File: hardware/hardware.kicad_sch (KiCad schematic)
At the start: 22 parts, among them J1 Screw_Terminal_01x02, J2 Screw_Terminal_01x02, J3 Screw_Terminal_01x02, K1 RM85-2011-35-1005, K2 RM85-2011-35-1005, Q1 BC337, Q2 BC337, U1 XIAO-ESP32-C6, U2 DS18B20

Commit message: Started working on PCB
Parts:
- removed D3, D4: LED, LED_THT:LED_D5.0mm, symbol Device:LED
- removed R7, R8: 100R, Resistor_THT:R_Axial_DIN0204_L3.6mm_D1.6mm_P7.62mm_Horizontal, symbol Device:R
- D1, D2: footprint Diode_THT:D_DO-41_SOD81_P10.16mm_Horizontal -> Diode_THT:D_A-405_P7.62mm_Horizontal

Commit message: Started working on new PCB layout
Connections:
- net RELAY_B_IN: now reaches K2.11 (COM_1)
- net RELAY_B_IN: now also J3.1 (Pin_1), K2.21 (COM_2)
- net RELAY_B_OUT: now reaches K2.14 (NO_1)
- net RELAY_B_OUT: now also J3.2 (Pin_2), K2.24 (NO_2)
- net RELAY_A_IN: now reaches J2.1 (Pin_1)
- net RELAY_A_IN: now also K1.11 (COM_1), K1.21 (COM_2)
- net RELAY_A_OUT: now reaches J2.2 (Pin_2)
- net RELAY_A_OUT: now also K1.14 (NO_1), K1.24 (NO_2)

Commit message: New layout with new screw terminals
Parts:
- J1, J2, J3: footprint Degson Electronics:SHDR2W100P0X500_1X2_1000X780X1020P -> Degson Electronics:DG1285002P14
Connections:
- net LED_A is gone; now on net TEMP_SENSOR_DATA: U1.3 (GPIO2/A2/D2)
- net RELAY_A_CTRL: now also U1.10 (GPIO20/D9/MISO); no longer U1.1 (GPIO0/A0/D0)
- net RELAY_B_CTRL: now also U1.9 (GPIO19/D8/SCK); no longer U1.2 (GPIO1/A1/D1)
- net TEMP_SENSOR_DATA: no longer U1.5 (GPIO22/D4/SDA)
- net LED_B: no longer names the net of U1.4 (GPIO21/D3)
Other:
- moved on the sheet: J1, J2, J3
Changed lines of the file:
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@@
 	(wire
 		(pts
-			(xy 44.45 39.37) (xy 50.8 39.37)
-		)
-		(stroke
-			(width 0)
-			(type default)
-		)
-	)
-	(wire
-		(pts
 			(xy 68.58 134.62) (xy 72.39 134.62)
 		)
@@
 	(wire
 		(pts
-			(xy 201.93 116.84) (xy 207.01 116.84)
+			(xy 179.07 107.95) (xy 184.15 107.95)
 		)
 		(stroke
@@
 	(wire
 		(pts
-			(xy 201.93 119.38) (xy 207.01 119.38)
+			(xy 179.07 110.49) (xy 184.15 110.49)
 		)
 		(stroke
@@
 	(wire
 		(pts
+			(xy 100.33 46.99) (xy 105.41 46.99)
+		)
+		(stroke
+			(width 0)
+			(type default)
+		)
+	)
+	(wire
+		(pts
 			(xy 99.06 74.93) (xy 104.14 74.93)
 		)
@@
 	(wire
 		(pts
-			(xy 201.93 144.78) (xy 207.01 144.78)
+			(xy 44.45 35.56) (xy 50.8 35.56)
 		)
 		(stroke
@@
 	(wire
 		(pts
-			(xy 201.93 129.54) (xy 207.01 129.54)
+			(xy 179.07 135.89) (xy 184.15 135.89)
 		)
 		(stroke
@@
 	(wire
 		(pts
-			(xy 44.45 35.56) (xy 50.8 35.56)
+			(xy 179.07 120.65) (xy 184.15 120.65)
+		)
+		(stroke
+			(width 0)
+			(type default)
+		)
+	)
+	(wire
+		(pts
+			(xy 100.33 43.18) (xy 105.41 43.18)
 		)
 		(stroke
@@
 	(wire
 		(pts
-			(xy 201.93 132.08) (xy 207.01 132.08)
+			(xy 179.07 123.19) (xy 184.15 123.19)
 		)
 		(stroke
@@
 	(wire
 		(pts
-			(xy 44.45 43.18) (xy 50.8 43.18)
-		)
-		(stroke
-			(width 0)
-			(type default)
-		)
-	)
-	(wire
-		(pts
 			(xy 121.92 35.56) (xy 121.92 31.75)
 		)
@@
 	(wire
 		(pts
-			(xy 201.93 142.24) (xy 207.01 142.24)
+			(xy 179.07 133.35) (xy 184.15 133.35)
 		)
 		(stroke
@@
 	(global_label "TEMP_SENSOR_DATA"
 		(shape input)
-		(at 44.45 43.18 180)
+		(at 44.45 35.56 180)
 		(fields_autoplaced yes)
 		(effects
@@
 		)
 		(property "Intersheetrefs" "${INTERSHEET_REFS}"
-			(at 22.7778 43.18 0)
+			(at 22.7778 35.56 0)
 			(effects
 				(font
@@
 	(global_label "230VAC_N"
 		(shape input)
-		(at 201.93 119.38 180)
+		(at 179.07 110.49 180)
 		(fields_autoplaced yes)
 		(effects
@@
 		)
 		(property "Intersheetrefs" "${INTERSHEET_REFS}"
-			(at 189.571 119.38 0)
+			(at 166.711 110.49 0)
 			(effects
 				(font
@@
 		)
 	)
-	(global_label "RELAY_B_CTRL"
-		(shape input)
-		(at 44.45 31.75 180)
-		(fields_autoplaced yes)
-		(effects
-			(font
-				(size 1.27 1.27)
-			)
-			(justify right)
-		)
-		(property "Intersheetrefs" "${INTERSHEET_REFS}"
-			(at 28.0996 31.75 0)
-			(effects
-				(font
-					(size 1.27 1.27)
-				)
-				(justify right)
-				(hide yes)
-			)
-		)
-	)
-	(global_label "LED_A"
-		(shape input)
-		(at 44.45 35.56 180)
-		(fields_autoplaced yes)
-		(effects
-			(font
-				(size 1.27 1.27)
-			)
-			(justify right)
-		)
-		(property "Intersheetrefs" "${INTERSHEET_REFS}"
-			(at 35.9615 35.56 0)
-			(effects
-				(font
-					(size 1.27 1.27)
-				)
-				(justify right)
-				(hide yes)
-			)
-		)
-	)
-	(global_label "LED_B"
+	(global_label "RELAY_B_OUT"
 		(shape input)
-		(at 44.45 39.37 180)
+		(at 31.75 134.62 180)
 		(fields_autoplaced yes)
 		(effects
@@
 		)
 		(property "Intersheetrefs" "${INTERSHEET_REFS}"
-			(at 35.7801 39.37 0)
+			(at 16.3067 134.62 0)
 			(effects
 				(font
@@
 		)
 	)
-	(global_label "RELAY_B_OUT"
+	(global_label "230VAC_L"
 		(shape input)
-		(at 31.75 134.62 180)
+		(at 179.07 107.95 180)
 		(fields_autoplaced yes)
 		(effects
@@
 		)
 		(property "Intersheetrefs" "${INTERSHEET_REFS}"
-			(at 16.3067 134.62 0)
+			(at 167.0134 107.95 0)
 			(effects
 				(font
@@
 		)
 	)
-	(global_label "230VAC_L"
+	(global_label "RELAY_B_IN"
 		(shape input)
-		(at 201.93 116.84 180)
+		(at 31.75 132.08 180)
 		(fields_autoplaced yes)
 		(effects
@@
 		)
 		(property "Intersheetrefs" "${INTERSHEET_REFS}"
-			(at 189.8734 116.84 0)
+			(at 18 132.08 0)
 			(effects
 				(font
@@
 		)
 	)
-	(global_label "RELAY_B_IN"
+	(global_label "RELAY_A_CTRL"
 		(shape input)
-		(at 31.75 132.08 180)
+		(at 105.41 43.18 0)
 		(fields_autoplaced yes)
 		(effects
@@
 				(size 1.27 1.27)
 			)
-			(justify right)
+			(justify left)
 		)
 		(property "Intersheetrefs" "${INTERSHEET_REFS}"
-			(at 18 132.08 0)
+			(at 121.579 43.18 0)
 			(effects
 				(font
 					(size 1.27 1.27)
 				)
-				(justify right)
+				(justify left)
 				(hide yes)
 			)
@@
 	(global_label "RELAY_A_IN"
 		(shape input)
-		(at 201.93 129.54 180)
+		(at 179.07 120.65 180)
 		(fields_autoplaced yes)
 		(effects
@@
 		)
 		(property "Intersheetrefs" "${INTERSHEET_REFS}"
-			(at 188.3614 129.54 0)
+			(at 165.5014 120.65 0)
 			(effects
 				(font
@@
 	(global_label "RELAY_B_IN"
 		(shape input)
-		(at 201.93 142.24 180)
+		(at 179.07 133.35 180)
 		(fields_autoplaced yes)
 		(effects
@@
 		)
 		(property "Intersheetrefs" "${INTERSHEET_REFS}"
-			(at 188.18 142.24 0)
+			(at 165.32 133.35 0)
 			(effects
 				(font
@@
 		)
 	)
-	(global_label "RELAY_A_CTRL"
+	(global_label "RELAY_B_CTRL"
 		(shape input)
-		(at 44.45 27.94 180)
+		(at 105.41 46.99 0)
 		(fields_autoplaced yes)
 		(effects
@@
 				(size 1.27 1.27)
 			)
-			(justify right)
+			(justify left)
 		)
 		(property "Intersheetrefs" "${INTERSHEET_REFS}"
-			(at 28.281 27.94 0)
+			(at 121.7604 46.99 0)
 			(effects
 				(font
 					(size 1.27 1.27)
 				)
-				(justify right)
+				(justify left)
 				(hide yes)
 			)
@@
 	(global_label "RELAY_B_OUT"
 		(shape input)
-		(at 201.93 144.78 180)
+		(at 179.07 135.89 180)
 		(fields_autoplaced yes)
 		(effects
@@
 		)
 		(property "Intersheetrefs" "${INTERSHEET_REFS}"
-			(at 186.4867 144.78 0)
+			(at 163.6267 135.89 0)
 			(effects
 				(font
@@
 	(global_label "RELAY_A_OUT"
 		(shape input)
-		(at 201.93 132.08 180)
+		(at 179.07 123.19 180)
 		(fields_autoplaced yes)
 		(effects
@@
 		)
 		(property "Intersheetrefs" "${INTERSHEET_REFS}"
-			(at 186.6681 132.08 0)
+			(at 163.8081 123.19 0)
 			(effects
 				(font
@@
 	(symbol
 		(lib_id "Connector:Screw_Terminal_01x02")
-		(at 212.09 129.54 0)
+		(at 189.23 120.65 0)
 		(unit 1)
 		(exclude_from_sim no)
@@
 		(fields_autoplaced yes)
 		(property "Reference" "J2"
-			(at 214.63 129.5399 0)
+			(at 191.77 120.6499 0)
 			(effects
 				(font
@@
 		)
 		(property "Value" "Screw_Terminal_01x02"
-			(at 214.63 132.0799 0)
+			(at 191.77 123.1899 0)
 			(effects
 				(font
@@
 			)
 		)
-		(property "Footprint" "Degson Electronics:SHDR2W100P0X500_1X2_1000X780X1020P"
-			(at 212.09 129.54 0)
+		(property "Footprint" "Degson Electronics:DG1285002P14"
+			(at 189.23 120.65 0)
 			(effects
 				(font
@@
 		)
 		(property "Datasheet" "~"
-			(at 212.09 129.54 0)
+			(at 189.23 120.65 0)
 			(effects
 				(font
@@
 		)
 		(property "Description" "Generic screw terminal, single row, 01x02, script generated (kicad-library-utils/schlib/autogen/connector/)"
-			(at 212.09 129.54 0)
+			(at 189.23 120.65 0)
 			(effects
 				(font
@@
 	(symbol
 		(lib_id "Connector:Screw_Terminal_01x02")
-		(at 212.09 116.84 0)
+		(at 189.23 107.95 0)
 		(unit 1)
 		(exclude_from_sim no)
@@
 		(fields_autoplaced yes)
 		(property "Reference" "J1"
-			(at 214.63 116.8399 0)
+			(at 191.77 107.9499 0)
 			(effects
 				(font
@@
 		)
 		(property "Value" "Screw_Terminal_01x02"
-			(at 214.63 119.3799 0)
+			(at 191.77 110.4899 0)
 			(effects
 				(font
@@
 			)
 		)
-		(property "Footprint" "Degson Electronics:SHDR2W100P0X500_1X2_1000X780X1020P"
-			(at 212.09 116.84 0)
+		(property "Footprint" "Degson Electronics:DG1285002P14"
+			(at 189.23 107.95 0)
 			(effects
 				(font
@@
 		)
 		(property "Datasheet" "~"
-			(at 212.09 116.84 0)
+			(at 189.23 107.95 0)
 			(effects
 				(font
@@
 		)
 		(property "Description" "Generic screw terminal, single row, 01x02, script generated (kicad-library-utils/schlib/autogen/connector/)"
-			(at 212.09 116.84 0)
+			(at 189.23 107.95 0)
 			(effects
 				(font
@@
 	(symbol
 		(lib_id "Connector:Screw_Terminal_01x02")
-		(at 212.09 142.24 0)
+		(at 189.23 133.35 0)
 		(unit 1)
 		(exclude_from_sim no)
@@
 		(fields_autoplaced yes)
 		(property "Reference" "J3"
-			(at 214.63 142.2399 0)
+			(at 191.77 133.3499 0)
 			(effects
 				(font
@@
 		)
 		(property "Value" "Screw_Terminal_01x02"
-			(at 214.63 144.7799 0)
+			(at 191.77 135.8899 0)
 			(effects
 				(font
@@
 			)
 		)
-		(property "Footprint" "Degson Electronics:SHDR2W100P0X500_1X2_1000X780X1020P"
-			(at 212.09 142.24 0)
+		(property "Footprint" "Degson Electronics:DG1285002P14"
+			(at 189.23 133.35 0)
 			(effects
 				(font
@@
 		)
 		(property "Datasheet" "~"
-			(at 212.09 142.24 0)
+			(at 189.23 133.35 0)
 			(effects
 				(font
@@
 		)
 		(property "Description" "Generic screw terminal, single row, 01x02, script generated (kicad-library-utils/schlib/autogen/connector/)"
-			(at 212.09 142.24 0)
+			(at 189.23 133.35 0)
 			(effects
 				(font

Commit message: Removed DS18B20 temp sensor
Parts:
- removed U2: DS18B20, Package_TO_SOT_THT:TO-92_Inline, symbol Sensor_Temperature:DS18B20
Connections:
- net RELAY_A_CTRL: now also U1.9 (GPIO19/D8/SCK); no longer U1.10 (GPIO20/D9/MISO)
- net RELAY_B_CTRL: now also U1.10 (GPIO20/D9/MISO); no longer U1.9 (GPIO19/D8/SCK)
- net TEMP_SENSOR_DATA: no longer names the net of U1.3 (GPIO2/A2/D2)

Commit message: Started working on PCB traces
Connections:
- net RELAY_A_CTRL: now also U1.1 (GPIO0/A0/D0); no longer U1.9 (GPIO19/D8/SCK)
- net RELAY_B_CTRL: now also U1.2 (GPIO1/A1/D1); no longer U1.10 (GPIO20/D9/MISO)
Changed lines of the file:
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@@
+	(wire
+		(pts
+			(xy 44.45 31.75) (xy 50.8 31.75)
+		)
+		(stroke
+			(width 0)
+			(type default)
+		)
+	)
 	(wire
 		(pts
@@
 	(wire
 		(pts
-			(xy 100.33 46.99) (xy 105.41 46.99)
+			(xy 44.45 27.94) (xy 50.8 27.94)
 		)
 		(stroke
@@
 	(wire
 		(pts
-			(xy 100.33 43.18) (xy 105.41 43.18)
-		)
-		(stroke
-			(width 0)
-			(type default)
-		)
-	)
-	(wire
-		(pts
 			(xy 111.76 116.84) (xy 116.84 116.84)
 		)
@@
 	(global_label "RELAY_A_CTRL"
 		(shape input)
-		(at 105.41 46.99 0)
-		(fields_autoplaced yes)
-		(effects
-			(font
-				(size 1.27 1.27)
-			)
-			(justify left)
-		)
-		(property "Intersheetrefs" "${INTERSHEET_REFS}"
-			(at 121.579 46.99 0)
-			(effects
-				(font
-					(size 1.27 1.27)
-				)
-				(justify left)
+		(at 44.45 27.94 180)
+		(fields_autoplaced yes)
+		(effects
+			(font
+				(size 1.27 1.27)
+			)
+			(justify right)
+		)
+		(property "Intersheetrefs" "${INTERSHEET_REFS}"
+			(at 28.281 27.94 0)
+			(effects
+				(font
+					(size 1.27 1.27)
+				)
+				(justify right)
 				(hide yes)
 			)
@@
 	(global_label "RELAY_B_CTRL"
 		(shape input)
-		(at 105.41 43.18 0)
-		(fields_autoplaced yes)
-		(effects
-			(font
-				(size 1.27 1.27)
-			)
-			(justify left)
-		)
-		(property "Intersheetrefs" "${INTERSHEET_REFS}"
-			(at 121.7604 43.18 0)
-			(effects
-				(font
-					(size 1.27 1.27)
-				)
-				(justify left)
-				(hide yes)
-			)
+		(at 44.45 31.75 180)
+		(fields_autoplaced yes)
+		(effects
+			(font
+				(size 1.27 1.27)
+			)
+			(justify right)
+		)
+		(property "Intersheetrefs" "${INTERSHEET_REFS}"
+			(at 28.0996 31.75 0)
+			(effects
+				(font
+					(size 1.27 1.27)
+				)
+				(justify right)
+				(hide yes)
+			)

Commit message: Removed unnecessary resistors
Removec resistors limiting current flowing through relay coils
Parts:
- removed R1, R3: 100R, Resistor_THT:R_Axial_DIN0204_L3.6mm_D1.6mm_P7.62mm_Horizontal, symbol Device:R
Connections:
- net at D2.2 (A), K2.A2 (COIL_2): now also Q2.1 (C)
- net at D1.2 (A), K1.A2 (COIL_2): now also Q1.1 (C)
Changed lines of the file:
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@@
 	(wire
 		(pts
-			(xy 72.39 85.09) (xy 78.74 85.09)
+			(xy 72.39 85.09) (xy 91.44 85.09)
 		)
 		(stroke
@@
 	(wire
 		(pts
-			(xy 86.36 127) (xy 91.44 127)
-		)
-		(stroke
-			(width 0)
-			(type default)
-		)
-	)
-	(wire
-		(pts
 			(xy 116.84 74.93) (xy 116.84 78.74)
 		)
@@
 	(wire
 		(pts
-			(xy 72.39 127) (xy 78.74 127)
+			(xy 72.39 127) (xy 91.44 127)
 		)
 		(stroke
@@
 		(pts
 			(xy 193.04 35.56) (xy 213.36 35.56)
-		)
-		(stroke
-			(width 0)
-			(type default)
-		)
-	)
-	(wire
-		(pts
-			(xy 86.36 85.09) (xy 91.44 85.09)
 		)
 		(stroke
@@
 	)
 	(symbol
-		(lib_id "Device:R")
-		(at 82.55 127 90)
-		(unit 1)
-		(exclude_from_sim no)
-		(in_bom yes)
-		(on_board yes)
-		(dnp no)
-		(fields_autoplaced yes)
-		(property "Reference" "R3"
-			(at 82.55 120.65 90)
-			(effects
-				(font
-					(size 1.27 1.27)
-				)
-			)
-		)
-		(property "Value" "100R"
-			(at 82.55 123.19 90)
-			(effects
-				(font
-					(size 1.27 1.27)
-				)
-			)
-		)
-		(property "Footprint" "Resistor_THT:R_Axial_DIN0204_L3.6mm_D1.6mm_P7.62mm_Horizontal"
-			(at 82.55 128.778 90)
-			(effects
-				(font
-					(size 1.27 1.27)
-				)
-				(hide yes)
-			)
-		)
-		(property "Datasheet" "~"
-			(at 82.55 127 0)
-			(effects
-				(font
-					(size 1.27 1.27)
-				)
-				(hide yes)
-			)
-		)
-		(property "Description" "Resistor"
-			(at 82.55 127 0)
-			(effects
-				(font
-					(size 1.27 1.27)
-				)
-				(hide yes)
-			)
-		)
-		(pin "2"
-		)
-		(pin "1"
-		)
-		(instances
-			(project "hardware"
-				(path "/75da26a7-4fdf-42c4-9276-67798e7ef829"
-					(reference "R3")
-					(unit 1)
-				)
-			)
-		)
-	)
-	(symbol
 		(lib_id "power:+3V3")
 		(at 121.92 31.75 0)
@@
 					(unit 1)
 				)
-			)
-		)
-	)
-	(symbol
-		(lib_id "Device:R")
-		(at 82.55 85.09 90)
-		(unit 1)
-		(exclude_from_sim no)
-		(in_bom yes)
-		(on_board yes)
-		(dnp no)
-		(fields_autoplaced yes)
-		(property "Reference" "R1"
-			(at 82.55 78.74 90)
-			(effects
-				(font
-					(size 1.27 1.27)
-				)
-			)
-		)
-		(property "Value" "100R"
-			(at 82.55 81.28 90)
-			(effects
-				(font
-					(size 1.27 1.27)
-				)
-			)
-		)
-		(property "Footprint" "Resistor_THT:R_Axial_DIN0204_L3.6mm_D1.6mm_P7.62mm_Horizontal"
-			(at 82.55 86.868 90)
-			(effects
-				(font
-					(size 1.27 1.27)
-				)
-				(hide yes)
-			)
-		)
-		(property "Datasheet" "~"
-			(at 82.55 85.09 0)
-			(effects
-				(font
-					(size 1.27 1.27)
-				)
-				(hide yes)
-			)
-		)
-		(property "Description" "Resistor"
-			(at 82.55 85.09 0)
-			(effects
-				(font
-					(size 1.27 1.27)
-				)
-				(hide yes)
-			)
-		)
-		(pin "2"
-		)
-		(pin "1"
-		)
-		(instances
-			(project "hardware"
-				(path "/75da26a7-4fdf-42c4-9276-67798e7ef829"
-					(reference "R1")
-					(unit 1)
-				)

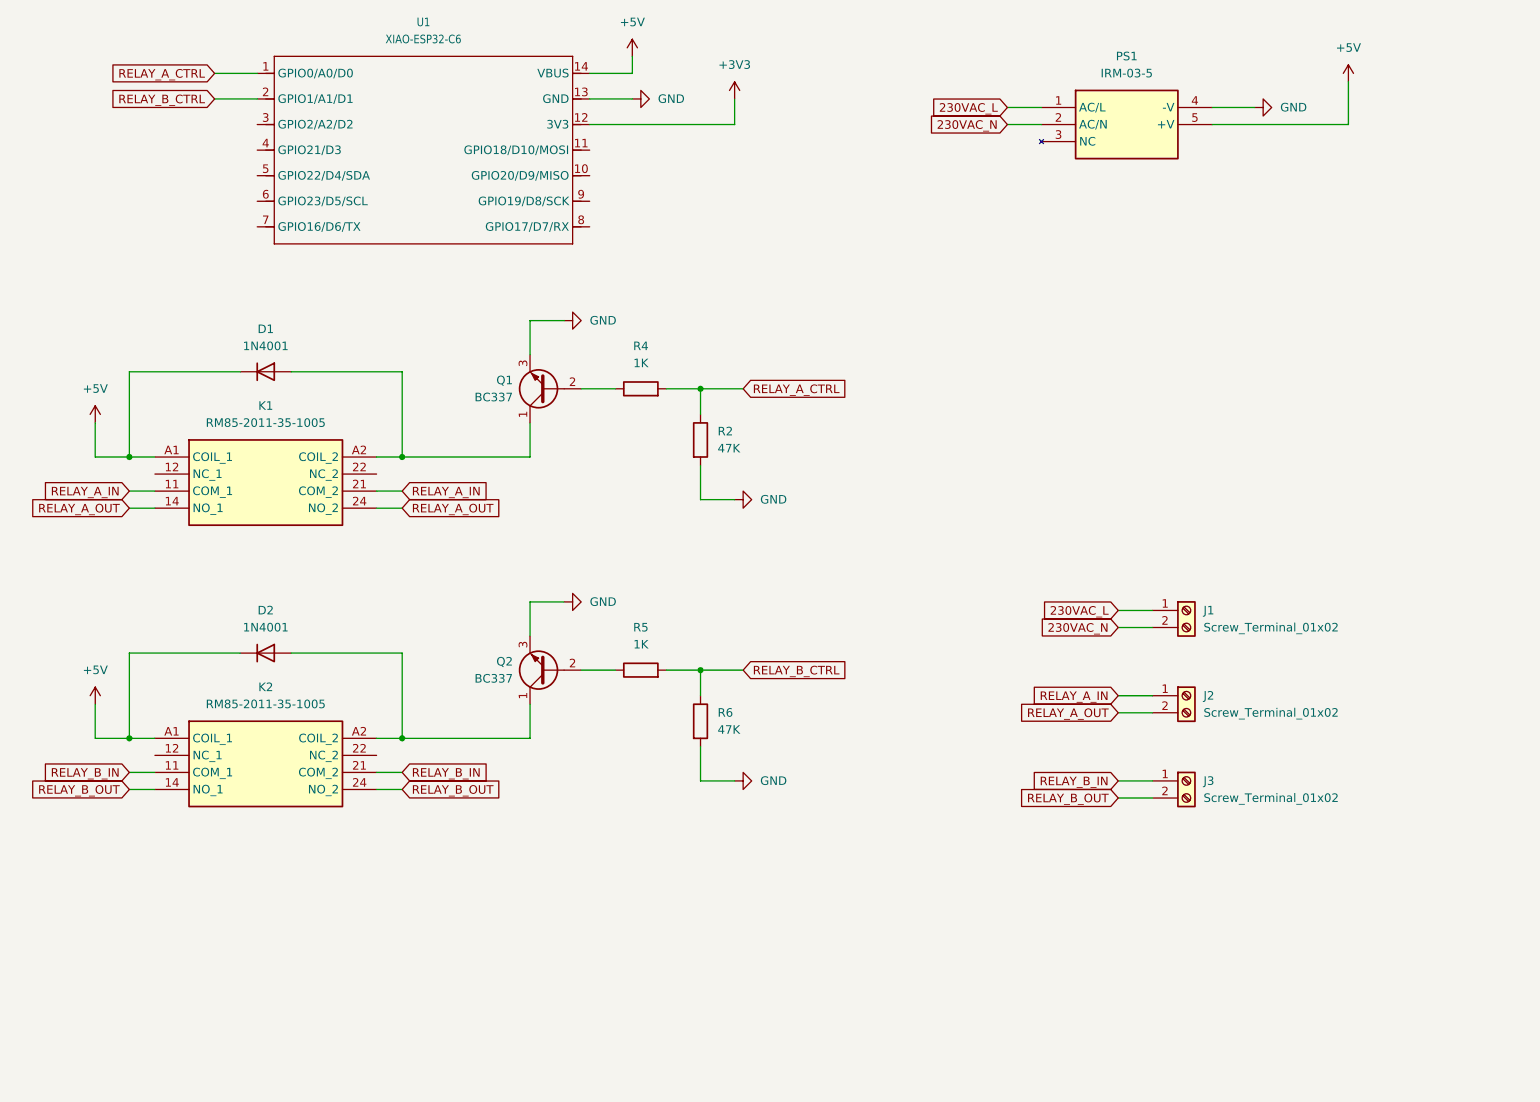
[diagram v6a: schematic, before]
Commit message: Updated PCB footprint layout
Updatec PCB layout after removing resistors
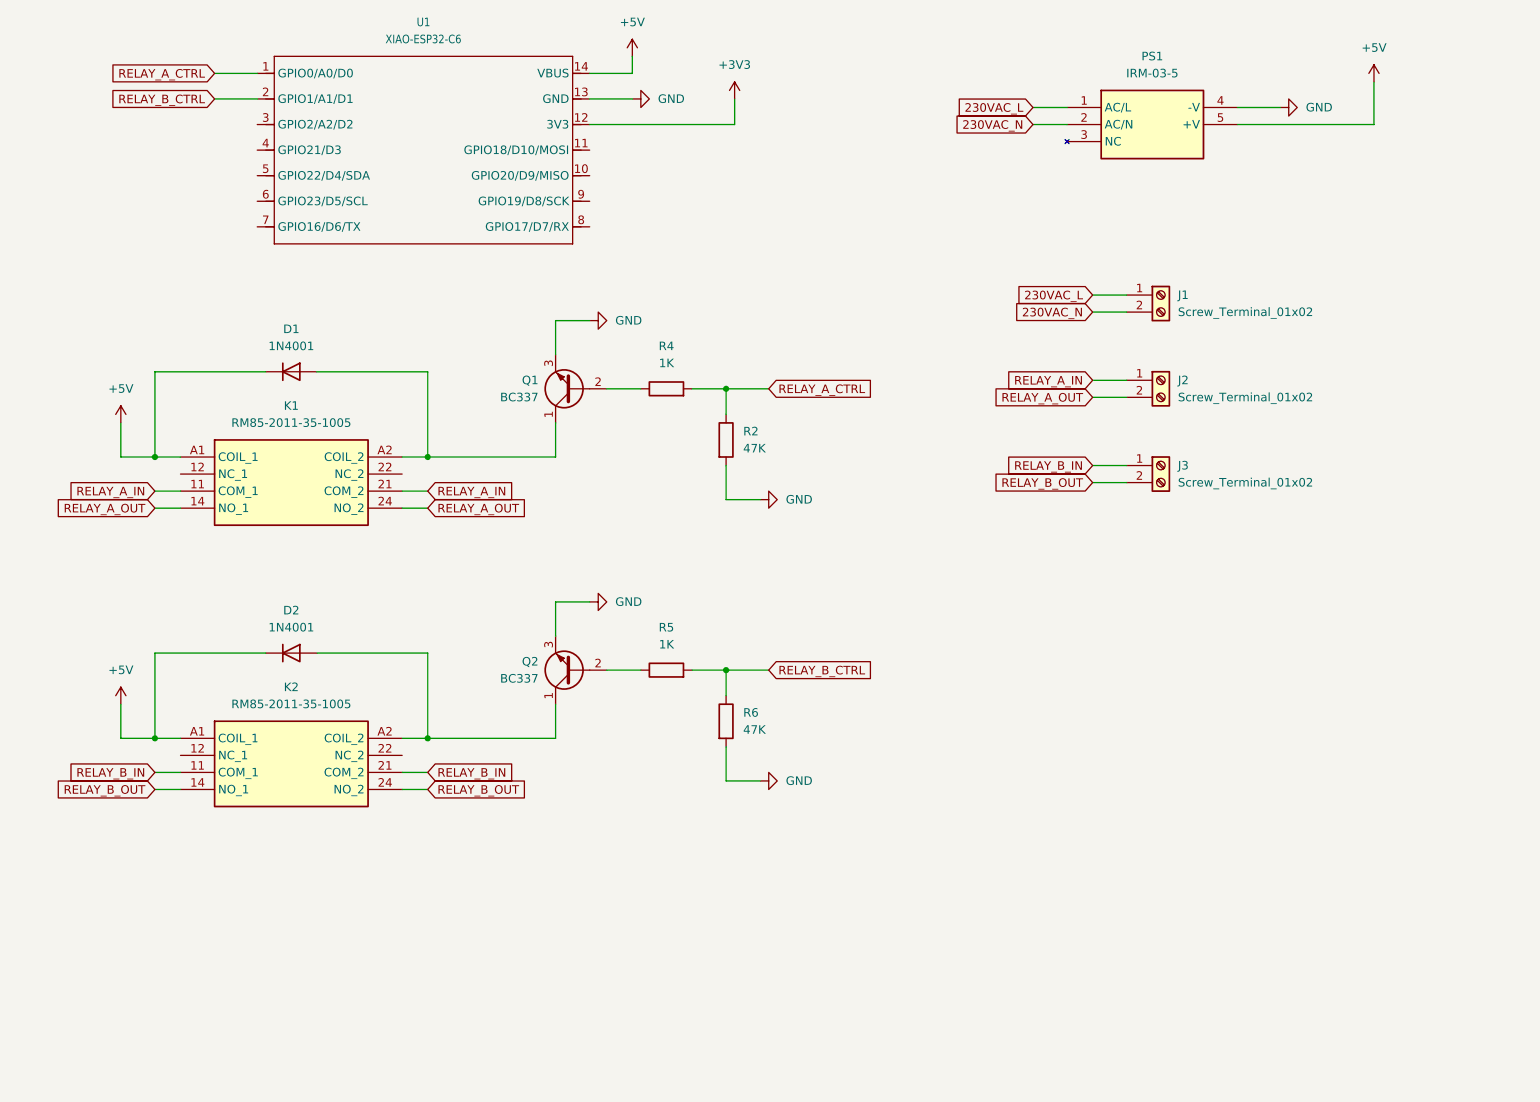
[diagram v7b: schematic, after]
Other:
- moved on the sheet: D1, D2, J1, J2, J3, K1, K2, PS1, Q1, Q2, R2, R4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
